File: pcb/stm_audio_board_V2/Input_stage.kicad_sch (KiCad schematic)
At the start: 23 parts, among them J7 GuitarIN, U3 AD1974, U4 OP275, Y1 Crystal_GND24

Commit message: Update AD1939_input_with_offset.asc, AD1939_input_with_offset.net, and 6 more files...
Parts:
- removed C18: 100p, Capacitor_SMD:C_0603_1608Metric_Pad1.08x0.95mm_HandSolder, symbol Device:C_Small
- added C18: 220p, Capacitor_SMD:C_0603_1608Metric_Pad1.08x0.95mm_HandSolder, symbol Device:C_Small
- added C18: 68n, Capacitor_SMD:C_0603_1608Metric_Pad1.08x0.95mm_HandSolder, symbol Device:C_Small
- added R4: 1Meg, Resistor_SMD:R_0805_2012Metric_Pad1.20x1.40mm_HandSolder, symbol Device:R
- added R4: 100, Resistor_SMD:R_0805_2012Metric_Pad1.20x1.40mm_HandSolder, symbol Device:R
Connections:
- net GNDA: now also C18.1
- net GUITAR_IN: now also R4.1; no longer R4.1, R4.2
- new net: C18.1, R4.2, R4.2
- new net: C18.2, C18.2, R4.1, R4.2
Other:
- moved on the sheet: C17, C19, C20, C21, C22, C23, C24, J7, R4, R5, R6, R7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

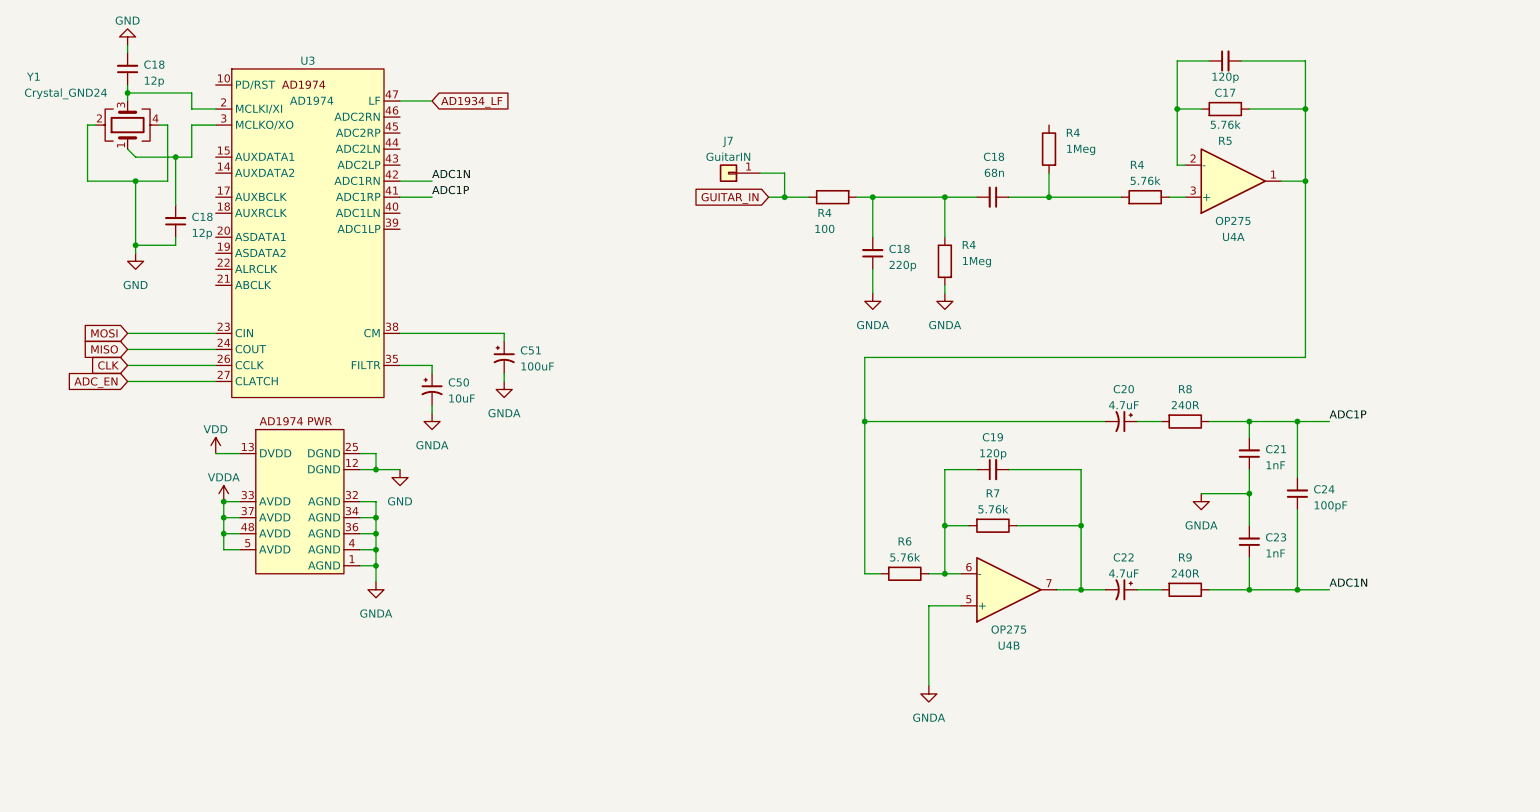
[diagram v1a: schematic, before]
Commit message: Update AD1939_input_with_offset.asc, AD1939_input_with_offset.log, and 8 more files...
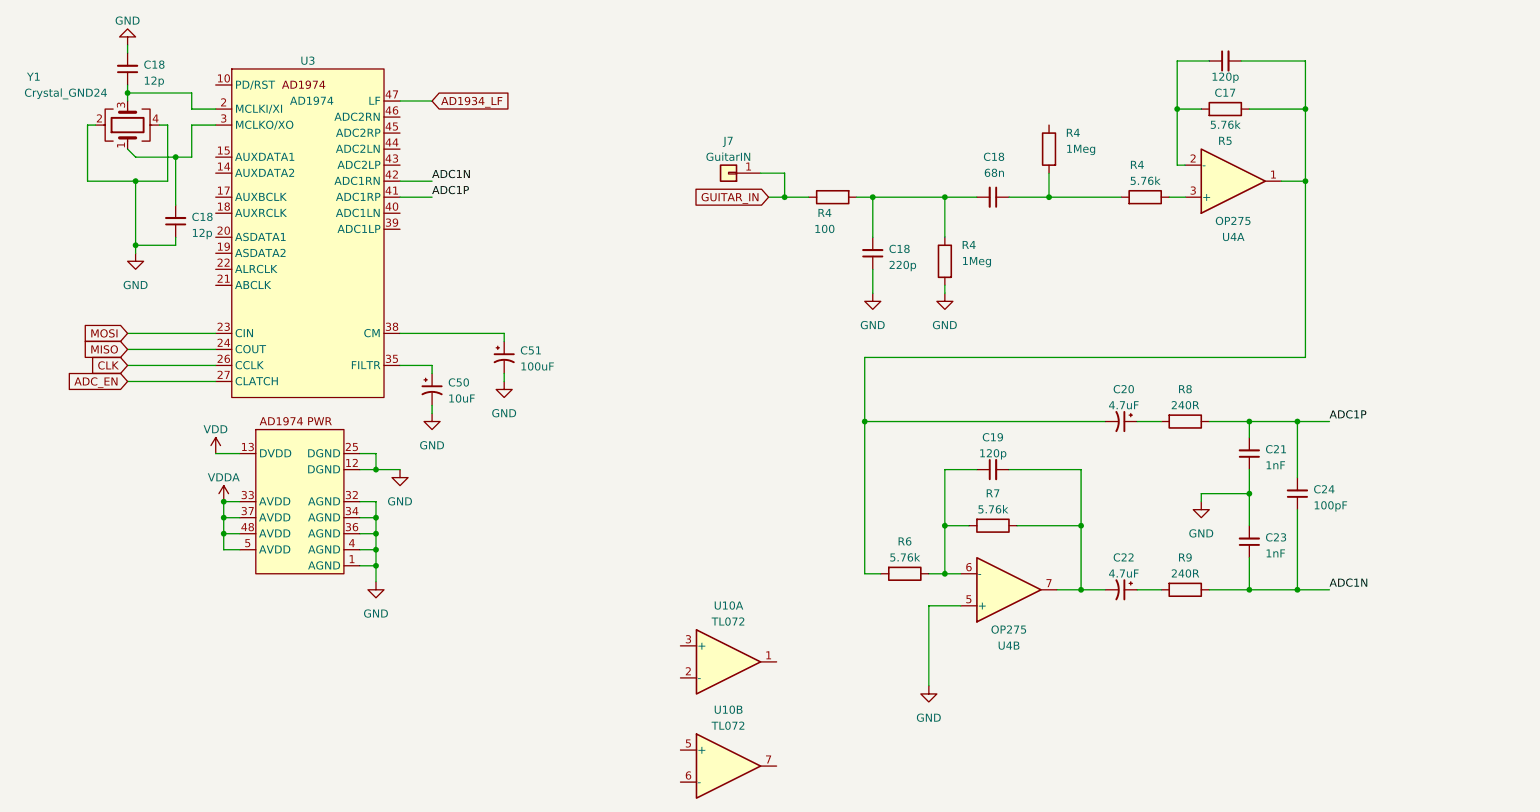
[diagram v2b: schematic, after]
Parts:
- added U10: TL072, symbol Amplifier_Operational:TL072
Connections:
- net GNDA is gone; now on net GND: C18.1, C21.1, C23.2, C50.2, C51.2, R4.2, U3.1 (AGND), U3.32 (AGND), U3.34 (AGND), U3.36 (AGND), U3.4 (AGND), U4.5 (+)

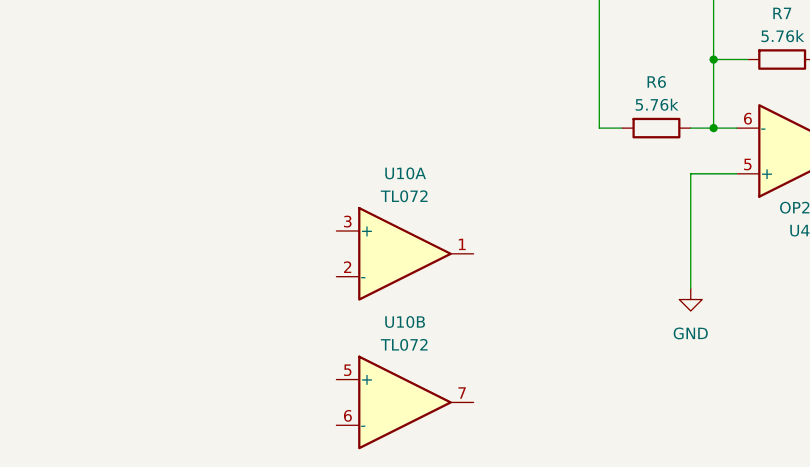
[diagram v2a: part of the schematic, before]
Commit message: ad1939 input stage update
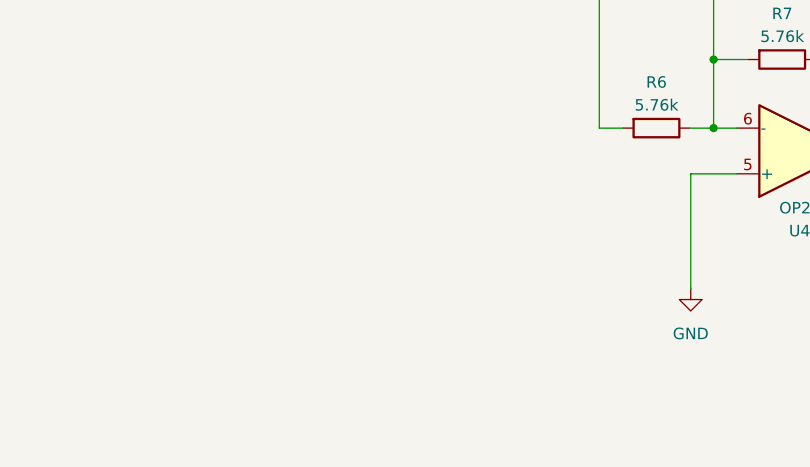
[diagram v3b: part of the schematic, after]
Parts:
- removed U10: TL072, symbol Amplifier_Operational:TL072
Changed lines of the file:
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@@
-    )
-  )
-  (symbol (lib_id "Amplifier_Operational:TL072") (at 124.46 144.78 0) (unit 1)
-    (in_bom yes) (on_board yes) (dnp no) (fields_autoplaced)
-    (property "Reference" "U10" (at 124.46 135.89 0)
-      (effects (font (size 1.27 1.27)))
-    )
-    (property "Value" "TL072" (at 124.46 138.43 0)
-      (effects (font (size 1.27 1.27)))
-    )
-    (property "Footprint" "" (at 124.46 144.78 0)
-      (effects (font (size 1.27 1.27)) hide)
-    )
-    (property "Datasheet" "http://www.ti.com/lit/ds/symlink/tl071.pdf" (at 124.46 144.78 0)
-      (effects (font (size 1.27 1.27)) hide)
-    )
-    (pin "1")
-    (pin "2")
-    (pin "3")
-    (pin "5")
-    (pin "6")
-    (pin "7")
-    (pin "4")
-    (pin "8")
-    (instances
-      (project "stm_audio_board_V2"
-        (path "/6997cf63-2615-4e49-9471-e7da1b6bae71/f20dc640-ad21-4977-8df1-611625087c69"
-          (reference "U10") (unit 1)
-        )
-      )
     )
   )
@@
         )
       )
-    )
-  )
-  (symbol (lib_id "Amplifier_Operational:TL072") (at 124.46 161.29 0) (unit 2)
-    (in_bom yes) (on_board yes) (dnp no) (fields_autoplaced)
-    (property "Reference" "U10" (at 124.46 152.4 0)
-      (effects (font (size 1.27 1.27)))
-    )
-    (property "Value" "TL072" (at 124.46 154.94 0)
-      (effects (font (size 1.27 1.27)))
-    )
-    (property "Footprint" "" (at 124.46 161.29 0)
-      (effects (font (size 1.27 1.27)) hide)
-    )
-    (property "Datasheet" "http://www.ti.com/lit/ds/symlink/tl071.pdf" (at 124.46 161.29 0)
-      (effects (font (size 1.27 1.27)) hide)
-    )
-    (pin "1")
-    (pin "2")
-    (pin "3")
-    (pin "5")
-    (pin "6")
-    (pin "7")
-    (pin "4")
-    (pin "8")
-    (instances
-      (project "stm_audio_board_V2"
-        (path "/6997cf63-2615-4e49-9471-e7da1b6bae71/f20dc640-ad21-4977-8df1-611625087c69"
-          (reference "U10") (unit 2)
-        )
-      )

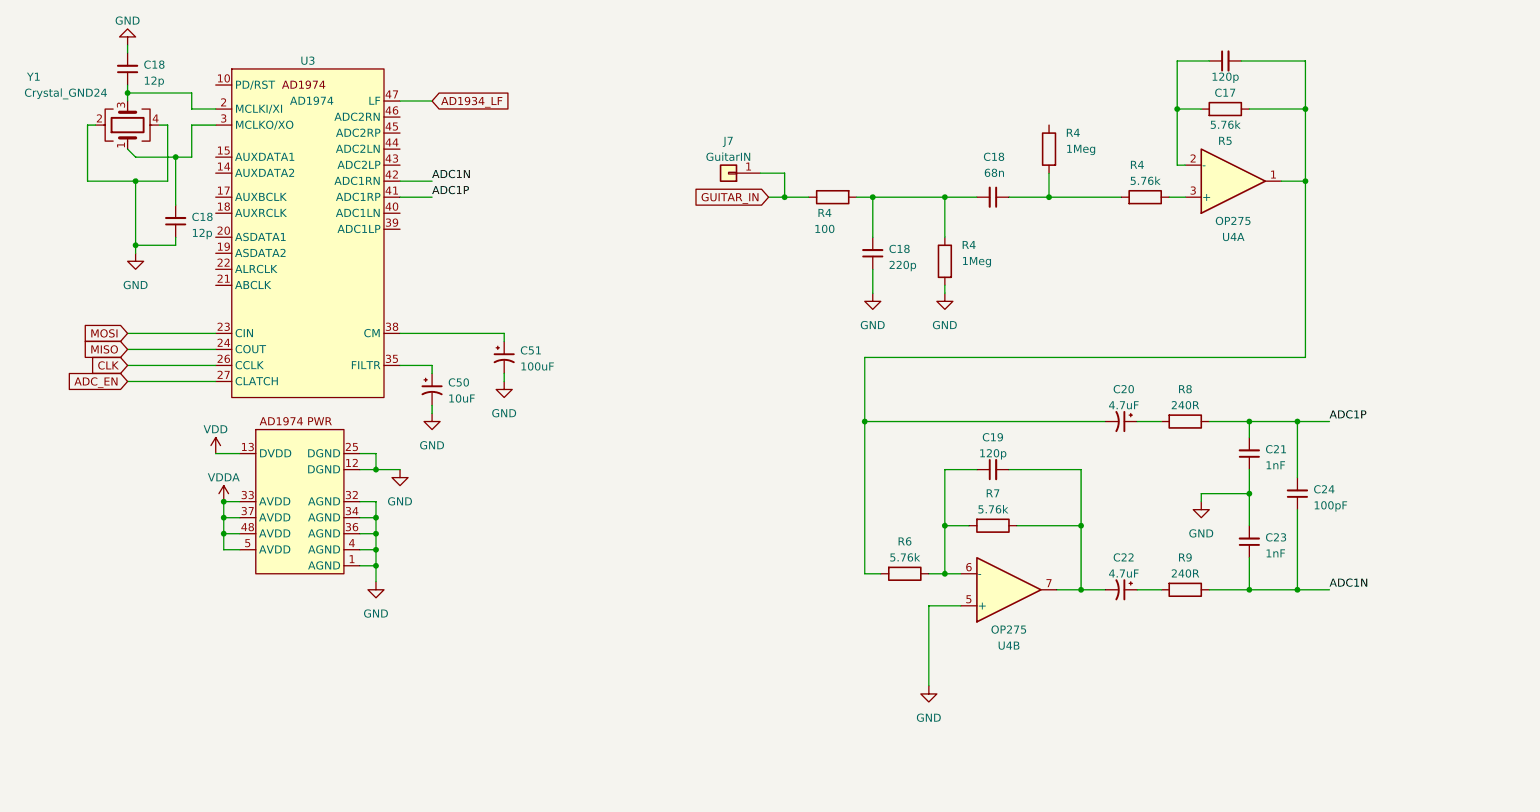
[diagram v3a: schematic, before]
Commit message: input and output stage reworked in sim and in schematic, power filtering is changed, further calculations needed
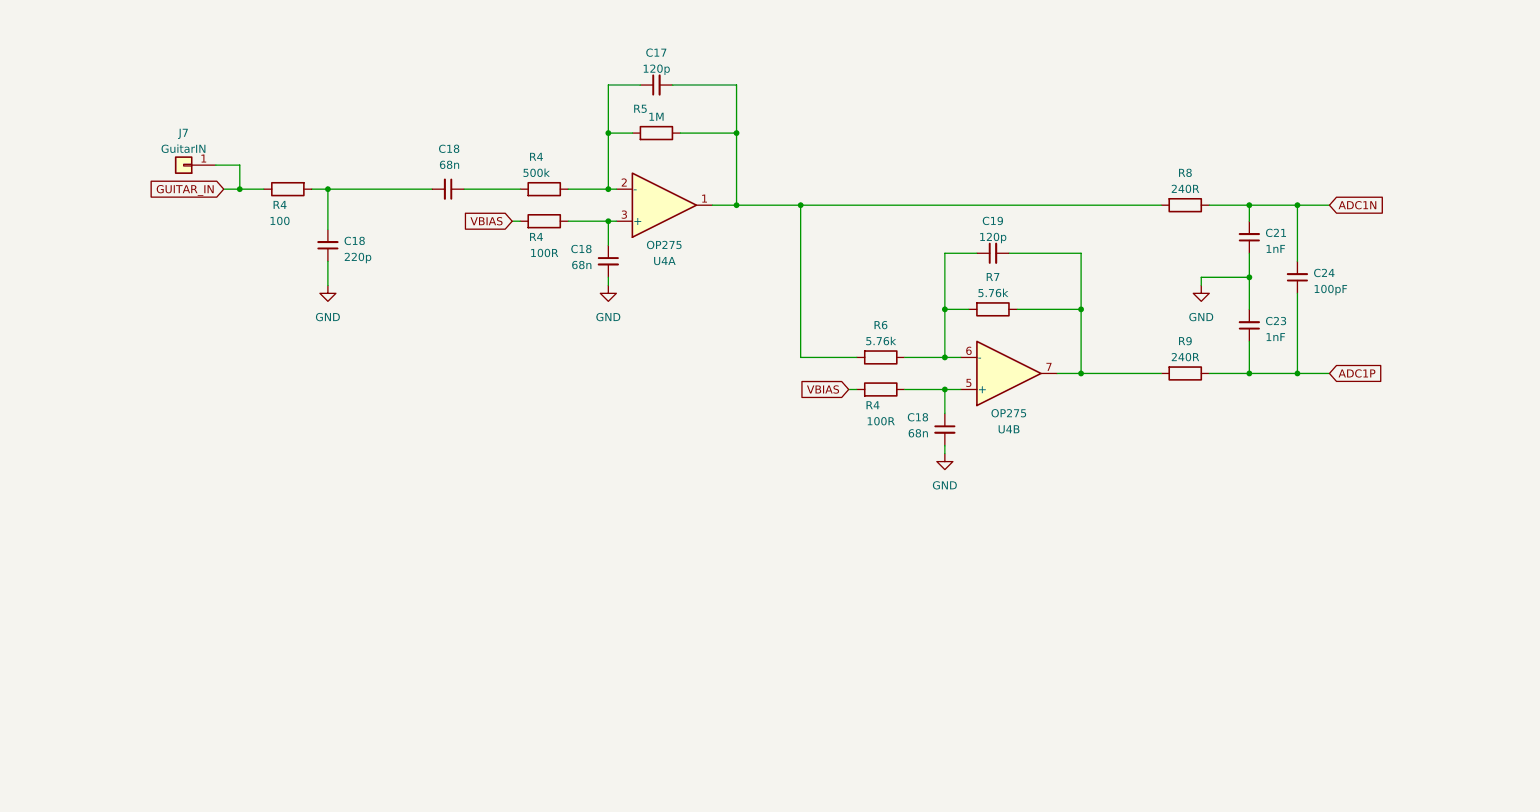
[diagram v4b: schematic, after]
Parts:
- removed C18 (x2): 12p, Capacitor_SMD:C_0603_1608Metric_Pad1.08x0.95mm_HandSolder, symbol Device:C_Small
- removed C20, C22: 4.7uF, Capacitor_SMD:C_0805_2012Metric_Pad1.18x1.45mm_HandSolder, symbol Device:C_Polarized_Small_US
- removed C50: 10uF, Capacitor_SMD:C_1210_3225Metric_Pad1.33x2.70mm_HandSolder, symbol Device:C_Polarized_Small_US
- removed C51: 100uF, Capacitor_SMD:C_1210_3225Metric_Pad1.33x2.70mm_HandSolder, symbol Device:C_Polarized_Small_US
- removed R4 (x2): 1Meg, Resistor_SMD:R_0805_2012Metric_Pad1.20x1.40mm_HandSolder, symbol Device:R
- removed U3: AD1974, Package_QFP:LQFP-48_7x7mm_P0.5mm, symbol stm_audio:AD1974
- removed Y1: Crystal_GND24, Crystal:Crystal_SMD_5032-4Pin_5.0x3.2mm, symbol Device:Crystal_GND24
- added C18 (x2): 68n, Capacitor_SMD:C_0603_1608Metric_Pad1.08x0.95mm_HandSolder, symbol Device:C_Small
- added R4 (x2): 100R, Resistor_SMD:R_0805_2012Metric_Pad1.20x1.40mm_HandSolder, symbol Device:R
- R4: value 5.76k -> 500k
- R5: value 5.76k -> 1M
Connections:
- net ADC1N: now also C21.2, C24.2, R8.1; no longer C23.1, C24.1, R9.1
- net ADC1P: now also C23.1, C24.1, R9.1; no longer C21.2, C24.2, R8.1
- net GND: now also C18.2, C18.2; no longer U4.5 (+)
- net at C19.2, R7.1, U4.7: now also R9.2
- net at R8.2: now also C17.2, R5.1, R6.2, U4.1
- net at R4.1: now also C17.1, R5.2, U4.2 (-); no longer U4.3 (+)
- new net: C18.1, R4.1, U4.5 (+)
- new net: C18.1, R4.1, U4.3 (+)
- new net VBIAS: R4.2, R4.2
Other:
- moved on the sheet: C17, C18, C19, C21, C23, C24, J7, R4, R5, R6, R7, R8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

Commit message: Update #auto_saved_files#, Connectors.kicad_sch, and 18 more files...
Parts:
- removed J7: GuitarIN, Connector_PinHeader_2.54mm:PinHeader_1x01_P2.54mm_Vertical, symbol Connector_Generic:Conn_01x01
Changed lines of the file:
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@@
   (junction (at 180.34 88.9) (diameter 0) (color 0 0 0 0)
   )
-  (junction (at 46.99 69.85) (diameter 0) (color 0 0 0 0)
-  )
   (wire (pts (xy 110.49 53.34) (xy 105.41 53.34))
     (stroke (width 0) (type default))
@@
     (stroke (width 0) (type default))
   )
-  (wire (pts (xy 44.45 69.85) (xy 46.99 69.85))
-    (stroke (width 0) (type default))
-  )
   (wire (pts (xy 207.01 83.82) (xy 207.01 88.9))
     (stroke (width 0) (type default))
@@
     (stroke (width 0) (type default))
   )
-  (wire (pts (xy 43.18 66.04) (xy 46.99 66.04))
-    (stroke (width 0) (type default))
-  )
   (wire (pts (xy 121.92 72.39) (xy 125.73 72.39))
     (stroke (width 0) (type default))
@@
     (stroke (width 0) (type default))
   )
-  (wire (pts (xy 46.99 66.04) (xy 46.99 69.85))
-    (stroke (width 0) (type default))
-  )
   (wire (pts (xy 60.96 81.28) (xy 60.96 85.09))
     (stroke (width 0) (type default))
@@
     (stroke (width 0) (type default))
   )
-  (wire (pts (xy 46.99 69.85) (xy 50.8 69.85))
+  (wire (pts (xy 44.45 69.85) (xy 50.8 69.85))
     (stroke (width 0) (type default))
   )
@@
         )
       )
-    )
-  )
-  (symbol (lib_id "Connector_Generic:Conn_01x01") (at 38.1 66.04 180) (unit 1)
-    (in_bom yes) (on_board yes) (dnp no) (fields_autoplaced)
-    (property "Reference" "J7" (at 38.1 60.96 0)
-      (effects (font (size 1.27 1.27)))
-    )
-    (property "Value" "GuitarIN" (at 38.1 63.5 0)
-      (effects (font (size 1.27 1.27)))
-    )
-    (property "Footprint" "Connector_PinHeader_2.54mm:PinHeader_1x01_P2.54mm_Vertical" (at 38.1 66.04 0)
-      (effects (font (size 1.27 1.27)) hide)
-    )
-    (property "Datasheet" "~" (at 38.1 66.04 0)
-      (effects (font (size 1.27 1.27)) hide)
-    )
-    (pin "1")
-    (instances
-      (project "stm_audio_board_V2"
-        (path "/6997cf63-2615-4e49-9471-e7da1b6bae71"
-          (reference "J7") (unit 1)
-        )
-        (path "/6997cf63-2615-4e49-9471-e7da1b6bae71/f20dc640-ad21-4977-8df1-611625087c69"
-          (reference "J7") (unit 1)
-        )
-      )
